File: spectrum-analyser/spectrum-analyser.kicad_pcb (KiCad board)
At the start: 2 copper layers, 50 x 95 mm, 40 parts, among them J1 Conn_Coaxial, J2 Conn_01x02, Q1 PMOS, Q2 PMOS, Q3 Q_PMOS_GSD, Q4 Q_NMOS_GSD, Q5 Q_NMOS_GSD, SW1 SW_SPDT, SW2 SW_UP, SW3 SW_RIGHT, SW4 SW_LEFT, SW5 SW_DOWN, U1 1.3" OLED, U2 ESP32-C3_Zero, U3 LM1117MP-3.3, U4 RX5808(V3.3), U5 AP9101CK6, U6 MCP73831-2-OT

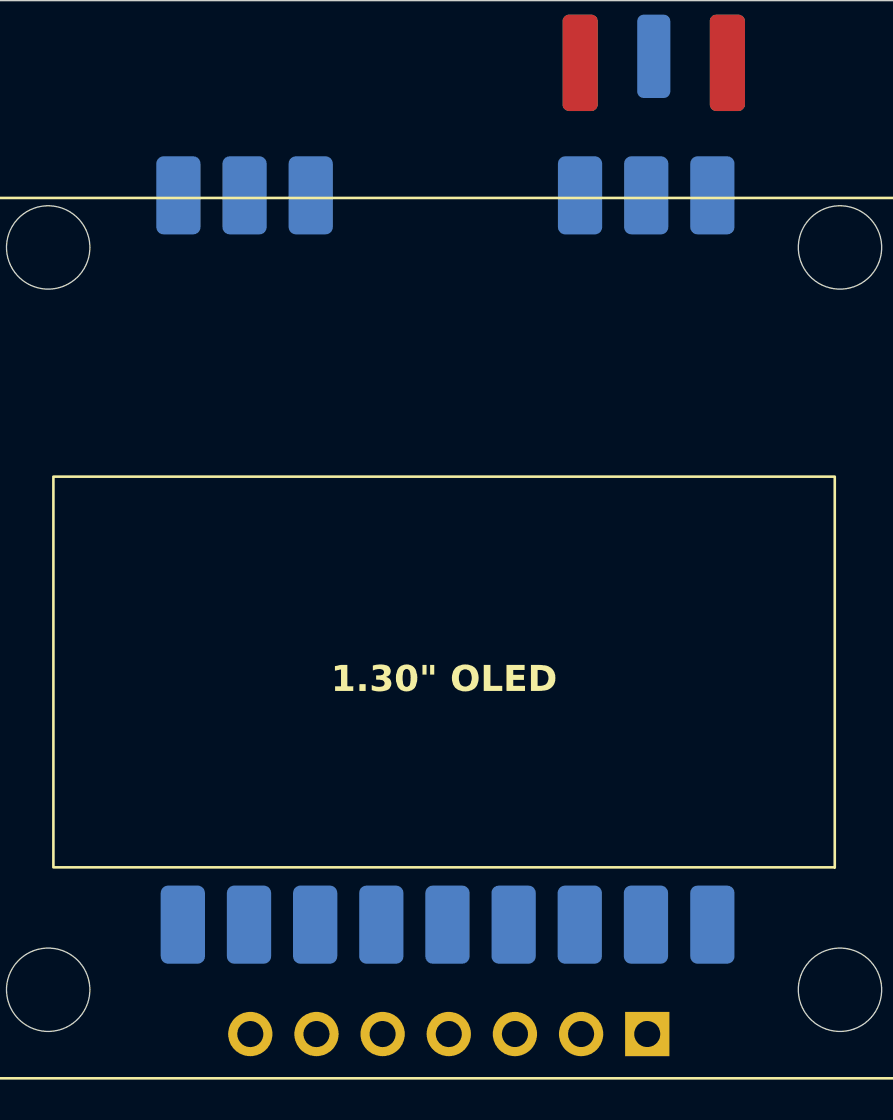
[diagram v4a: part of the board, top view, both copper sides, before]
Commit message: Add GND keepout around SMA and adjust thermal relief spoke angle for RX module
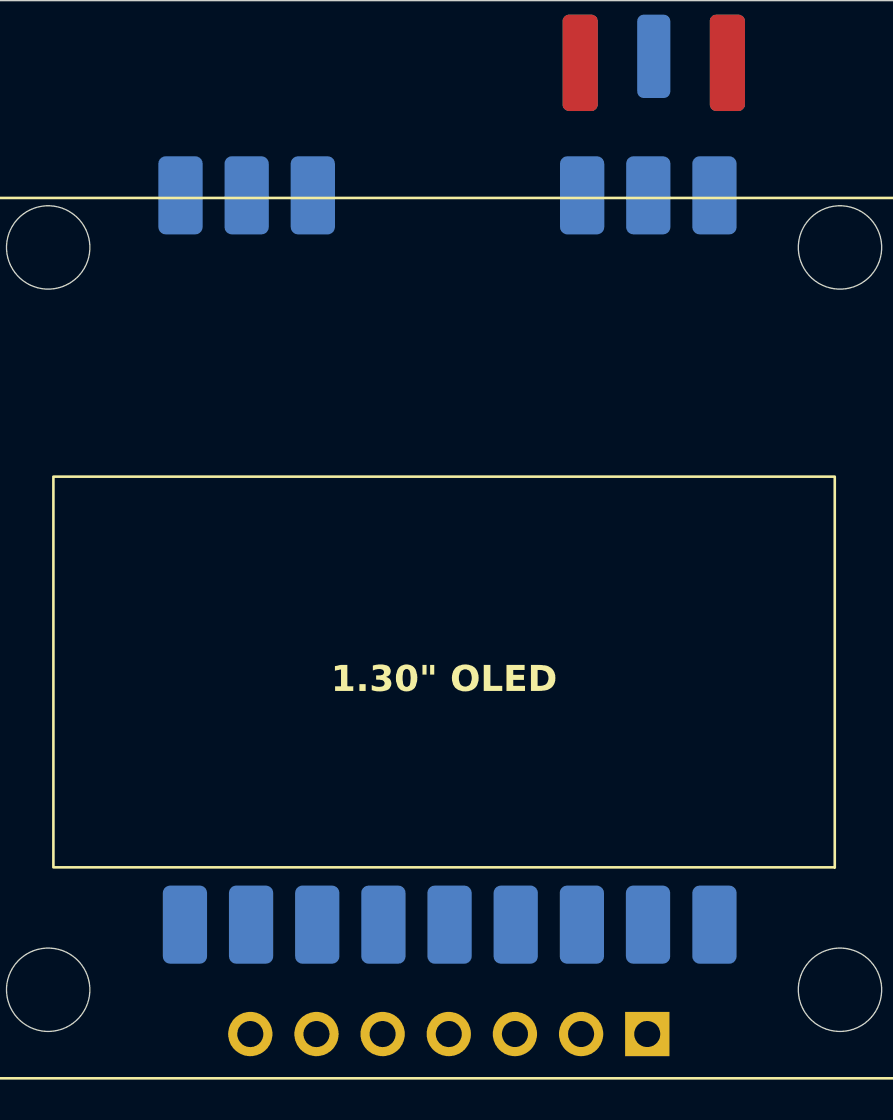
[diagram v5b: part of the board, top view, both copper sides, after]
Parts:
- moved U4 0.08 mm to (132.1, 67.5)
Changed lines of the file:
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@@
 		(tags "resistor handsolder")
 		(property "Reference" "R3"
-			(at -2.75 0 360)
+			(at -2.75 0 0)
 			(layer "F.SilkS")
 			(effects
@@
 		)
 		(property "Value" "150k"
-			(at 0 1.43 360)
+			(at 0 1.43 0)
 			(layer "F.Fab")
 			(effects
@@
 		)
 		(fp_text user "${REFERENCE}"
-			(at 0 0 360)
+			(at 0 0 0)
 			(layer "F.Fab")
 			(effects
@@
 		(tags "fuse handsolder")
 		(property "Reference" "F1"
-			(at -3 0 360)
+			(at -3 0 0)
 			(layer "F.SilkS")
 			(effects
@@
 		)
 		(property "Value" "Fuse"
-			(at 0 1.43 360)
+			(at 0 1.43 0)
 			(layer "F.Fab")
 			(effects
@@
 		(tags "solder jumper open")
 		(property "Reference" "JP1"
-			(at -4 -1.25 360)
+			(at -4 -1.25 0)
 			(layer "F.SilkS")
 			(effects
@@
 		)
 		(property "Value" "BAT_PROT_BYPASS"
-			(at 0 1.9 360)
+			(at 0 1.9 0)
 			(layer "F.Fab")
 			(effects
@@
 	(footprint "Thanassis_Foot:RX5808(V3.3)"
 		(layer "B.Cu")
-		(at 132 67.5 180)
+		(at 132.08 67.5 180)
 		(property "Reference" "U4"
 			(at 25.54 -25.45 -90)
@@
 		)
 		(property "Value" "RX5808(V3.3)"
-			(at 12.05 -10.8 0)
+			(at 11.25 7.75 0)
 			(unlocked yes)
 			(layer "B.Fab")
@@
 			(pinfunction "DATA")
 			(pintype "bidirectional")
-			(thermal_bridge_angle 45)
+			(thermal_bridge_angle 0)
 		)
 		(pad "2" smd roundrect
@@
 			(pinfunction "LE")
 			(pintype "input")
-			(thermal_bridge_angle 45)
+			(thermal_bridge_angle 0)
 		)
 		(pad "3" smd roundrect
@@
 			(pinfunction "CLK")
 			(pintype "input")
-			(thermal_bridge_angle 45)
+			(thermal_bridge_angle 0)
 		)
 		(pad "4" smd roundrect
@@
 			(pinfunction "GND")
 			(pintype "power_in")
-			(thermal_bridge_angle 45)
+			(thermal_bridge_angle 0)
 		)
 		(pad "5" smd roundrect
@@
 			(pinfunction "+5V")
 			(pintype "power_in")
-			(thermal_bridge_angle 45)
+			(thermal_bridge_angle 0)
 		)
 		(pad "6" smd roundrect
@@
 			(pinfunction "RSSI")
 			(pintype "output")
-			(thermal_bridge_angle 45)
+			(thermal_bridge_angle 0)
 		)
 		(pad "7" smd roundrect
@@
 			(pinfunction "A_6.5M")
 			(pintype "output+no_connect")
-			(thermal_bridge_angle 45)
+			(thermal_bridge_angle 0)
 		)
 		(pad "8" smd roundrect
@@
 			(pinfunction "VIDEO")
 			(pintype "output+no_connect")
-			(thermal_bridge_angle 45)
+			(thermal_bridge_angle 0)
 		)
 		(pad "9" smd roundrect
@@
 			(pinfunction "GND")
 			(pintype "power_in")
-			(thermal_bridge_angle 45)
+			(thermal_bridge_angle 0)
 		)
 		(pad "10" smd roundrect
@@
 			(pinfunction "GND")
 			(pintype "power_in")
-			(thermal_bridge_angle 45)
+			(thermal_bridge_angle 0)
 		)
 		(pad "11" smd roundrect
@@
 			(pinfunction "GND")
 			(pintype "power_in")
-			(thermal_bridge_angle 45)
+			(thermal_bridge_angle 0)
 		)
 		(pad "12" smd roundrect
@@
 			(pinfunction "GND")
 			(pintype "power_in")
-			(thermal_bridge_angle 45)
+			(thermal_bridge_angle 0)
 		)
 		(pad "13" smd roundrect
@@
 			(pinfunction "GND")
 			(pintype "power_in")
-			(thermal_bridge_angle 45)
+			(thermal_bridge_angle 0)
 		)
 		(pad "14" smd roundrect
@@
 			(pinfunction "ANT")
 			(pintype "input")
-			(thermal_bridge_angle 45)
+			(thermal_bridge_angle 0)
 		)
 		(pad "15" smd roundrect
@@
 			(pinfunction "GND")
 			(pintype "power_in")
-			(thermal_bridge_angle 45)
+			(thermal_bridge_angle 0)
 		)
 	)
@@
 	)
 	(zone
+		(net 0)
+		(net_name "")
+		(layer "B.Cu")
+		(name "RF GND keepout")
+		(hatch edge 0.5)
+		(connect_pads
+			(clearance 0)
+		)
+		(min_thickness 0.25)
+		(filled_areas_thickness no)
+		(keepout
+			(tracks not_allowed)
+			(vias not_allowed)
+			(pads not_allowed)
+			(copperpour not_allowed)
+			(footprints allowed)
+		)
+		(fill
+			(thermal_gap 0.5)
+			(thermal_bridge_width 0.5)
+		)
+		(polygon
+			(pts
+				(xy 122.5 70.5) (xy 133.25 70.5) (xy 133.25 59.25) (xy 122.5 59.25)
+			)
+		)
+	)
+	(zone

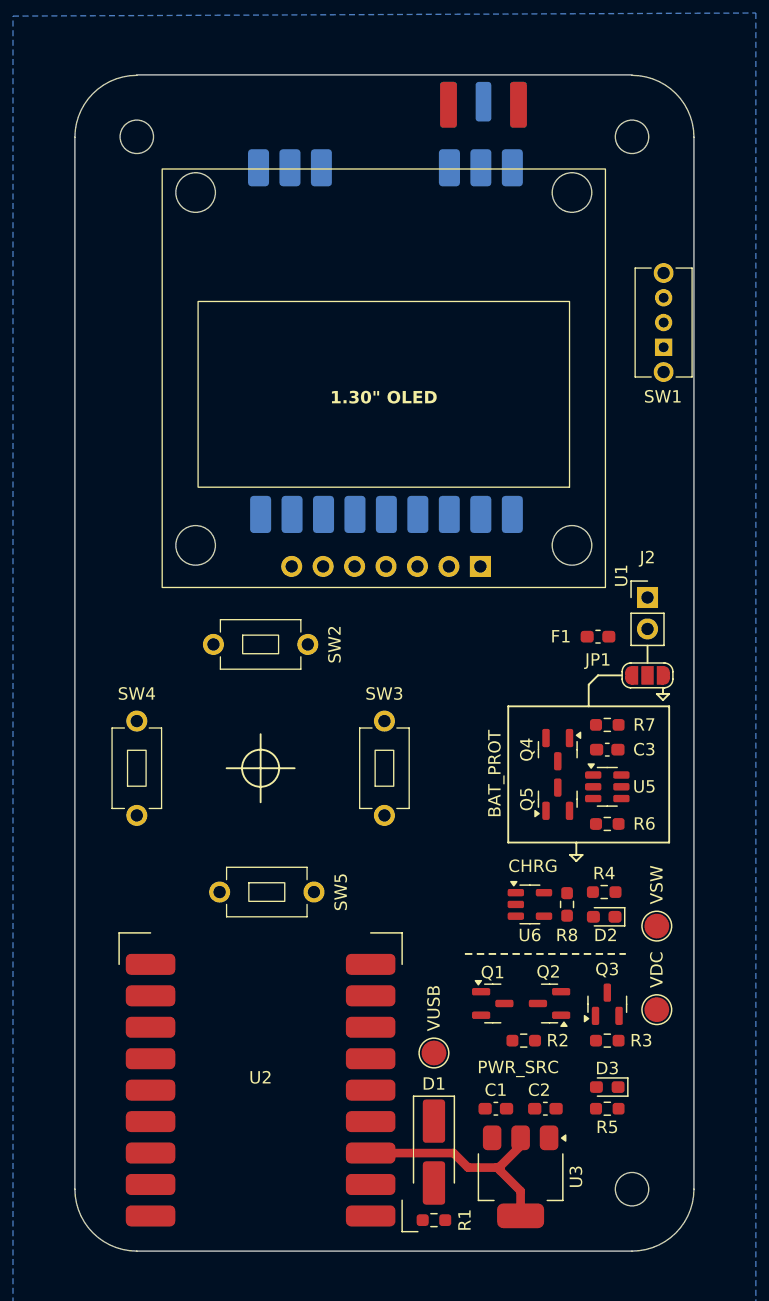
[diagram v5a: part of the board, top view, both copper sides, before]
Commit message: Route the power management sections
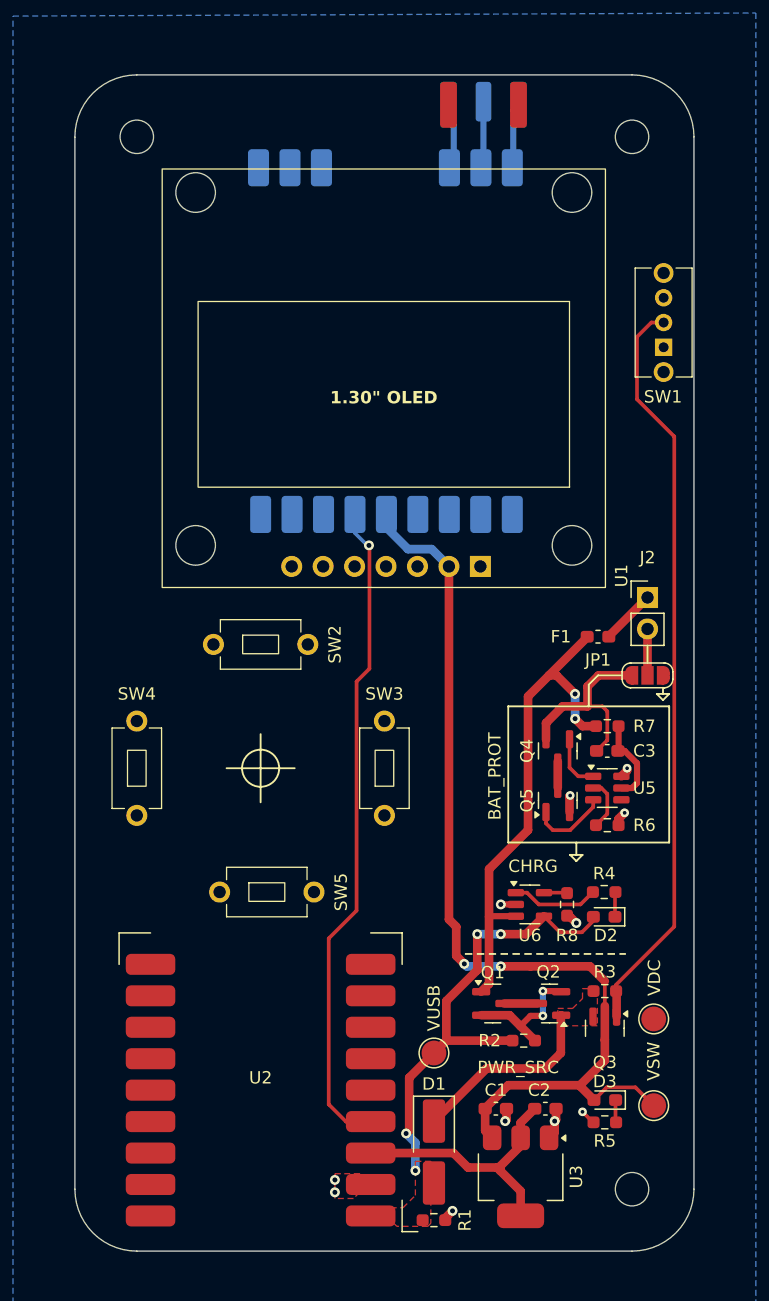
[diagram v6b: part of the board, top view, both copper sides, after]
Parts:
- moved TP3 14.5 mm to (141.8, 143.2)
- moved R3 4.00 mm to (137.8, 134.0), turned to 0 degrees
- moved Q3 1.95 mm to (137.8, 137.0), turned to -90 degrees
- moved R5 1.12 mm to (137.8, 144.6)
- moved D3 1.07 mm to (137.8, 142.8)
- moved TP2 0.79 mm to (141.8, 136.2)
- moved C3 0.10 mm to (138.0, 114.6)
- moved Q4 0.10 mm to (134.0, 114.6)
- moved Q5 0.10 mm to (134.0, 118.6)
- moved R6 0.10 mm to (138.0, 120.6)
- moved R7 0.10 mm to (138.0, 112.6)
- moved U5 0.10 mm to (138.0, 117.6)
- turned R2 to 0 degrees
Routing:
- net +VSW: track 0.00 -> 79.8 mm, vias 0 -> 2
- net /PWR_SW: track 0.00 -> 60.7 mm
- net RSSI: track 0.00 -> 53.5 mm, vias 0 -> 1
- net +BATT: track 0.00 -> 41.1 mm, vias 0 -> 2
- net VUSB: track 0.00 -> 38.4 mm, vias 0 -> 4
- net GND: track 0.00 -> 22.1 mm, vias 0 -> 11
- net -BAT_PROT: track 0.00 -> 16.1 mm
- net VDC: track 0.00 -> 15.6 mm
- net /PWR_SRC_SW_G: track 0.00 -> 10.9 mm, vias 0 -> 2
- net CHRG_STAT: track 0.00 -> 7.03 mm
- net /Battery management/BAT_PROT_VDD: track 0.00 -> 7.00 mm
- net /Battery management/BAT_PROT_CO: track 0.00 -> 6.31 mm
- net Net-(J1-In): track 0.00 -> 5.42 mm
- net /Battery management/BAT_PROT_DO: track 0.00 -> 4.49 mm
- net /Battery management/BAT_CONN_POS: track 0.00 -> 4.46 mm
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- added copper zone on F.Cu, net GND
- added copper zone on F.Cu, net VDC
- added copper zone on F.Cu, net VUSB

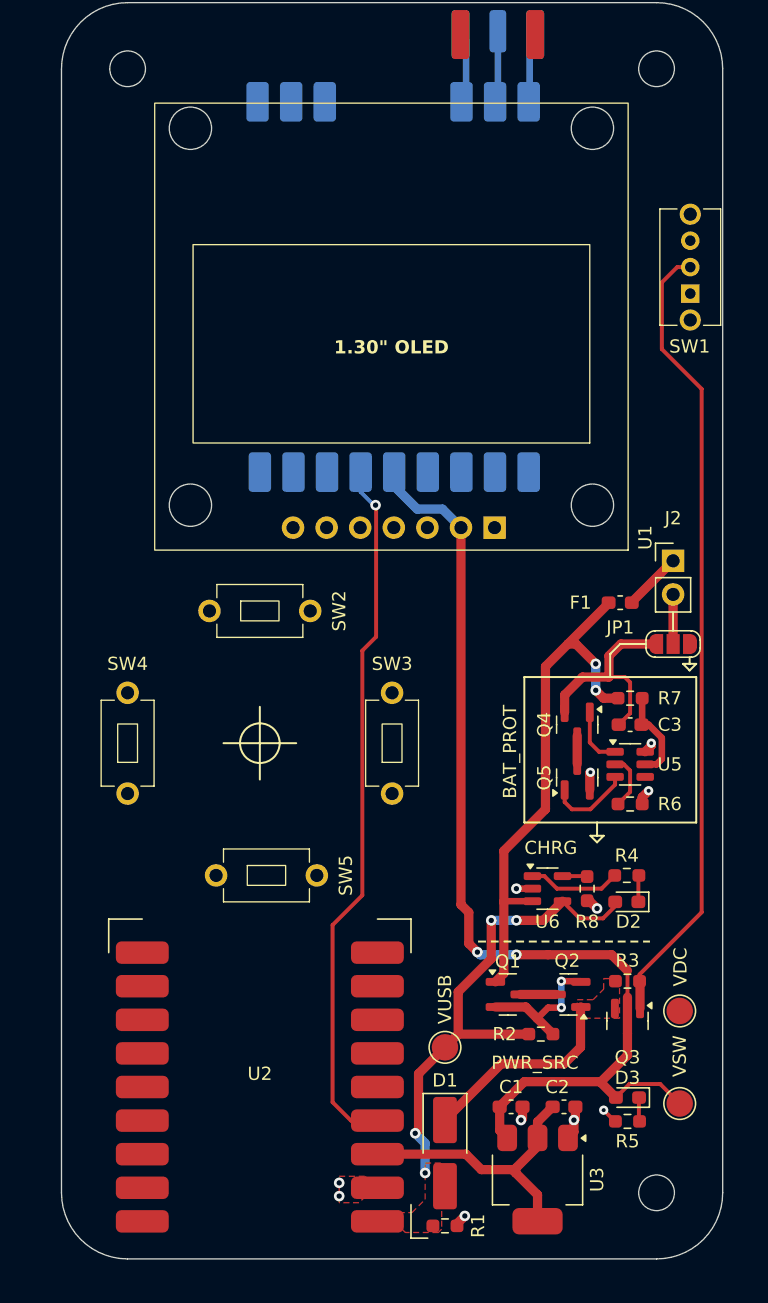
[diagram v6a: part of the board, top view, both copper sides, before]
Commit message: Route signal traces and adjust mcu module pin assignment
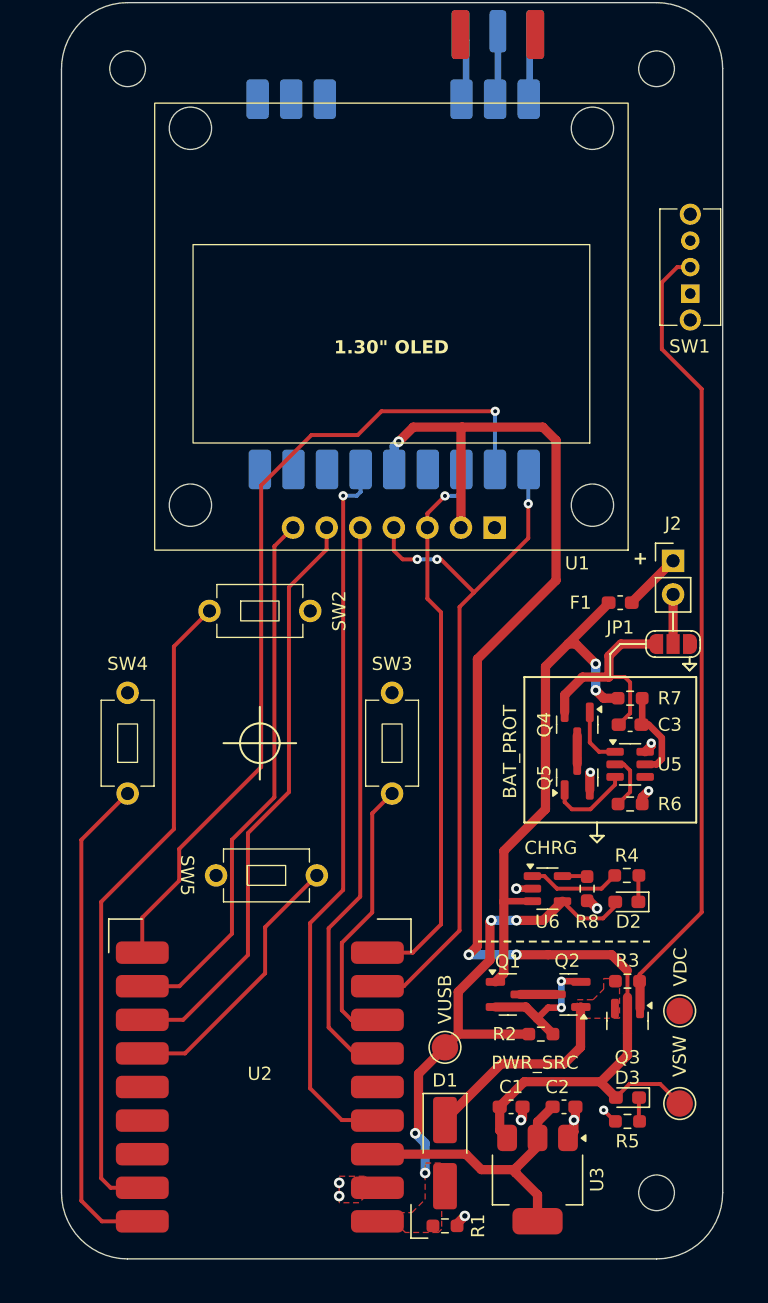
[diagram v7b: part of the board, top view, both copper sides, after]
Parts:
- moved U4 0.20 mm to (132.1, 67.3)
- turned SW5 to 180 degrees
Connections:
- U2 pad 10: DISPLAY_CS -> RX_CS
- U2 pad 11: RX_CS -> DISPLAY_CS
- U2 pad 12: DISPLAY_RST -> DISPLAY_DC
- U2 pad 13: DISPLAY_DC -> BTN_DOWN
- U2 pad 18: BTN_RIGHT -> BTN_LEFT
- U2 pad 6: BTN_DOWN -> DISPLAY_RST
- U2 pad 7: BTN_LEFT -> BTN_RIGHT
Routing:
- net RX_CS: track 0.00 -> 63.5 mm, vias 0 -> 1
- net SPI_MOSI: track 0.00 -> 54.1 mm, vias 0 -> 3
- net BTN_UP: track 0.00 -> 49.7 mm
- net DISPLAY_DC: track 0.00 -> 44.8 mm
- net DISPLAY_RST: track 0.00 -> 43.3 mm
- net SPI_CLK: track 0.00 -> 42.1 mm, vias 0 -> 1
- net DISPLAY_CS: track 0.00 -> 41.0 mm
- net BTN_LEFT: track 0.00 -> 37.5 mm
- net +VSW: track 79.8 -> 104.8 mm, vias 2 -> 3
- net BTN_RIGHT: track 0.00 -> 21.0 mm
- net BTN_DOWN: track 0.00 -> 20.8 mm
- net RSSI: track 53.5 -> 54.9 mm
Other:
- board text added: "+"
